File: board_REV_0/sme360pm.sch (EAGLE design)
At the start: 56 parts, among them J1 USB3075-30-A, P1 HEADER, P2 JTAG, SW1 TL3342F160QG/TR, U1 RT9193-33GB, U2 STM32F103C8T6, U3 MCP2551-I/SN, X1 87438-03, X2 87438-03, X3 87438-03, X4 87438-03, Y2 8MHz, Y3 32.768k

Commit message: Updated board
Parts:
- renumbered X1 to ENC1, X2 to ENC2, X3 to ENC3, X4 to ENC4

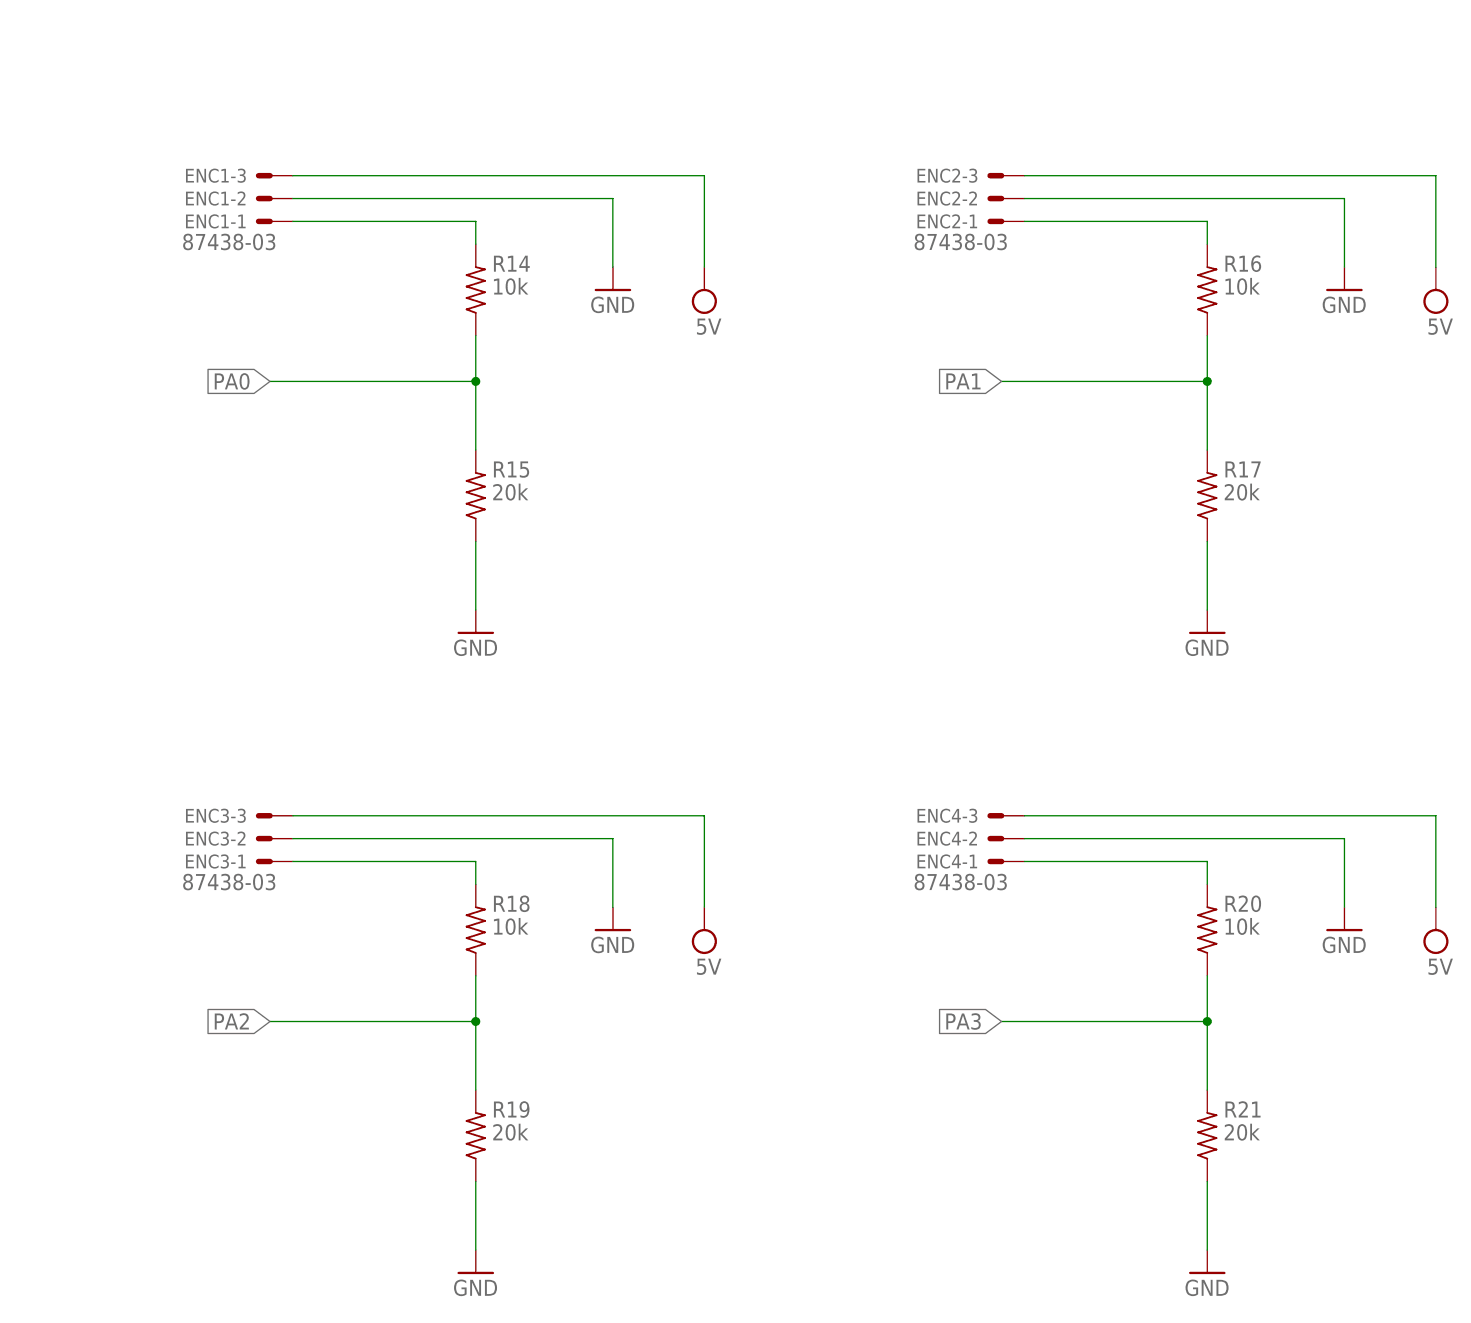
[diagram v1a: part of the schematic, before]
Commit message: Removed voltage divider
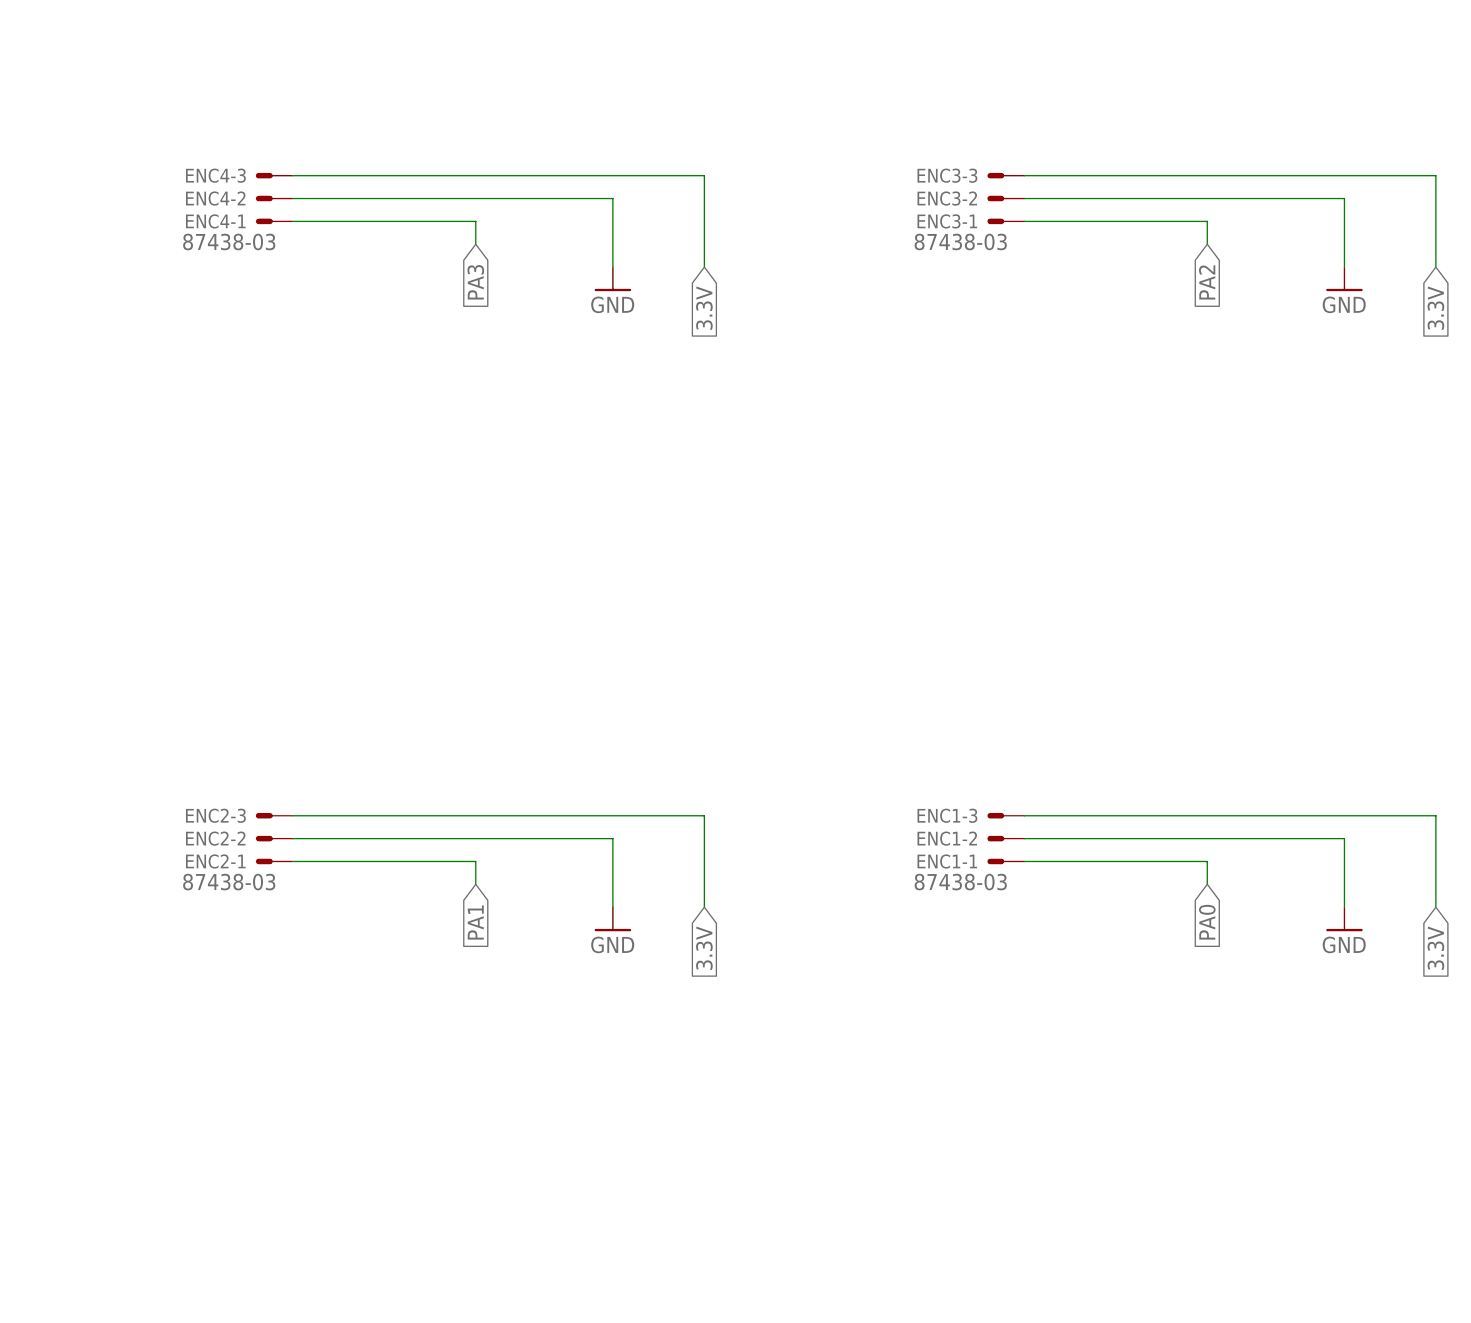
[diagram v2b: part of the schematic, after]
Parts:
- removed R14, R16, R18, R20: 10k, rcl:R-US_R0603
- removed R15, R17, R19, R21: 20k, rcl:R-US_R0603
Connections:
- removed net N$16: ENC1-1.S, R14.2
- removed net N$17: ENC2-1.S, R16.2
- removed net N$18: ENC3-1.S, R18.2
- removed net N$19: ENC4-1.S, R20.2
- net 3.3V: now also ENC1-3.S, ENC2-3.S, ENC3-3.S, ENC4-3.S
- net GND: no longer R15.1, R17.1, R19.1, R21.1
- net PA0: now also ENC1-1.S; no longer R14.1, R15.2
- net PA1: now also ENC2-1.S; no longer R16.1, R17.2
- net PA2: now also ENC3-1.S; no longer R18.1, R19.2
- net PA3: now also ENC4-1.S; no longer R20.1, R21.2
- net VCC: no longer ENC1-3.S, ENC2-3.S, ENC3-3.S, ENC4-3.S
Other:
- moved on the sheet: ENC1-1, ENC1-2, ENC1-3, ENC2-1, ENC2-2, ENC2-3, ENC3-1, ENC3-2, ENC3-3, ENC4-1, ENC4-2, ENC4-3
